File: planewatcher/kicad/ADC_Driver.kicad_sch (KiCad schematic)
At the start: 27 parts, among them U10 AD8138, U12 ADA4807-1, U3 OPA320

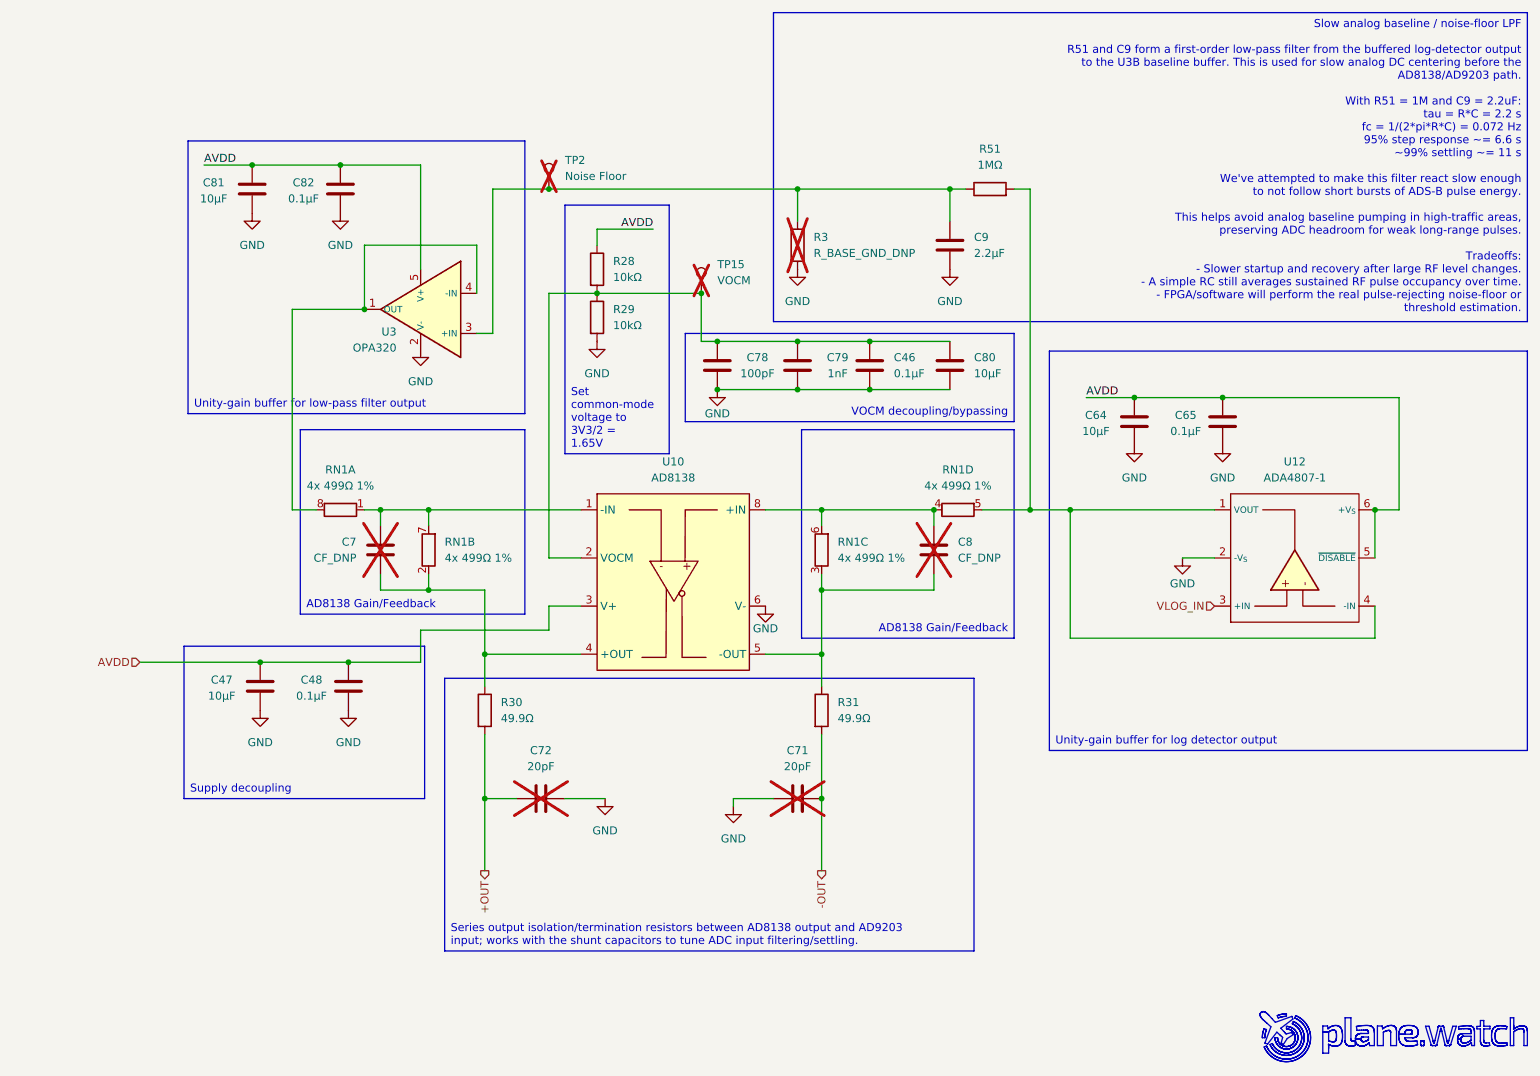
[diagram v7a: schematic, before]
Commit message: Add comments & markup to schematic
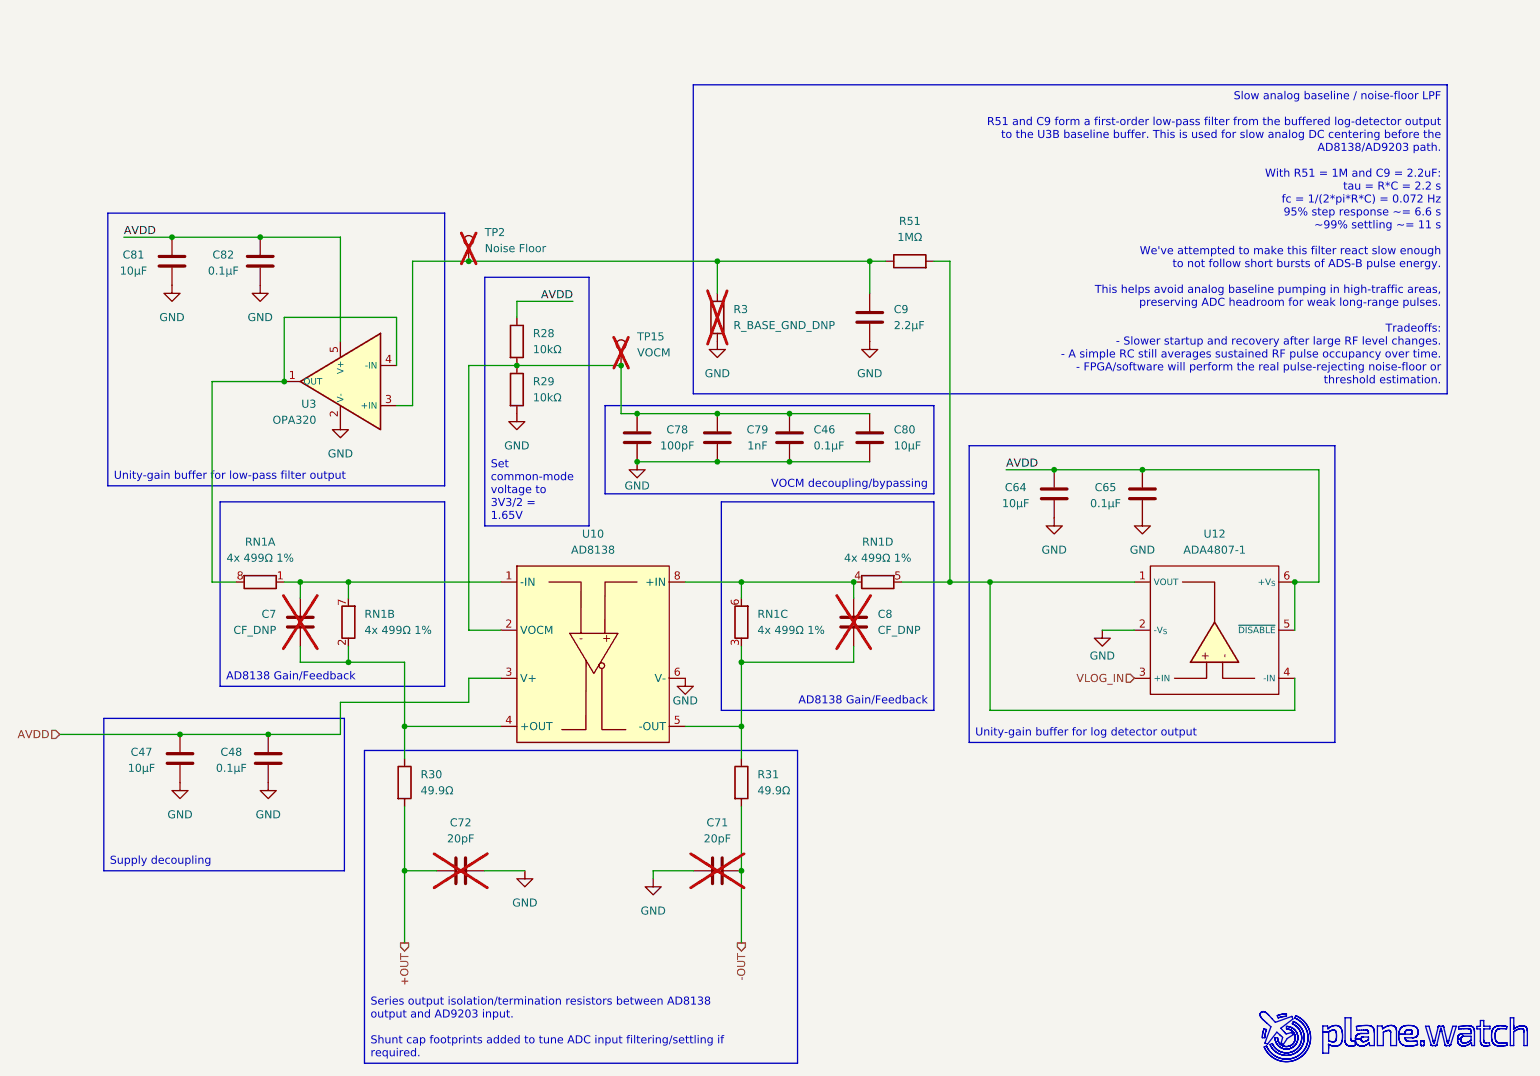
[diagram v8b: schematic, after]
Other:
- moved on the sheet: C46, C47, C48, C64, C65, C7, C71, C72, C78, C79, C8, C80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
